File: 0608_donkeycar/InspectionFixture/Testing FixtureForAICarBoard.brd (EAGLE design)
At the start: 65 x 56.5 mm, 100 parts, among them CON1 RASPBERRYPI_SHEILD, CON2 5077CR-16-SMC2-BK-TR, U1 RP2350A, U2 W25Q32RVXHJQ, U3 TXB0104, U4 RT6150B-33GQW, U5 DMG1012T, U6 MCP3008

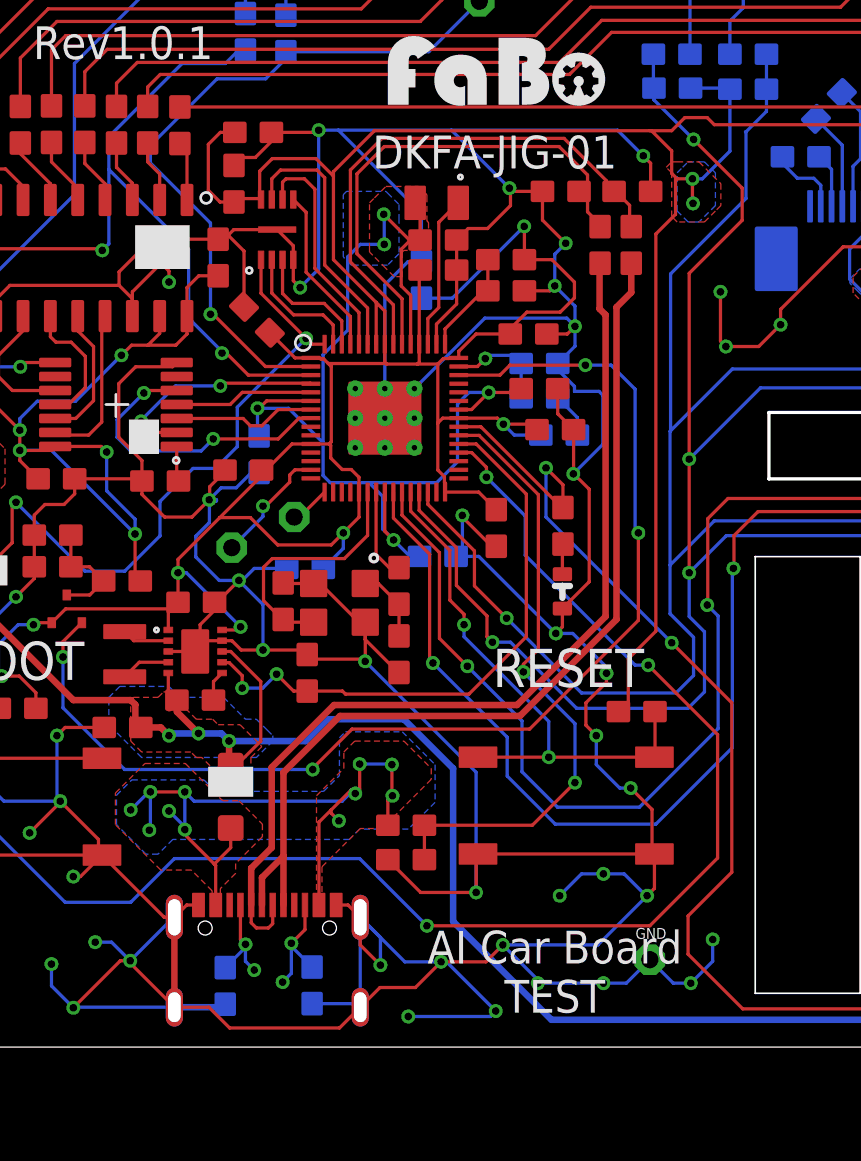
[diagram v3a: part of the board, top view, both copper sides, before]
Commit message: #608 AI Car Board Inspection Board Rev1.0.1 C34コンデンサ47uF追加、発振器マーキングポイント追加、アナログ系の電源の定数を変更、レベル変換A側電源断線修正
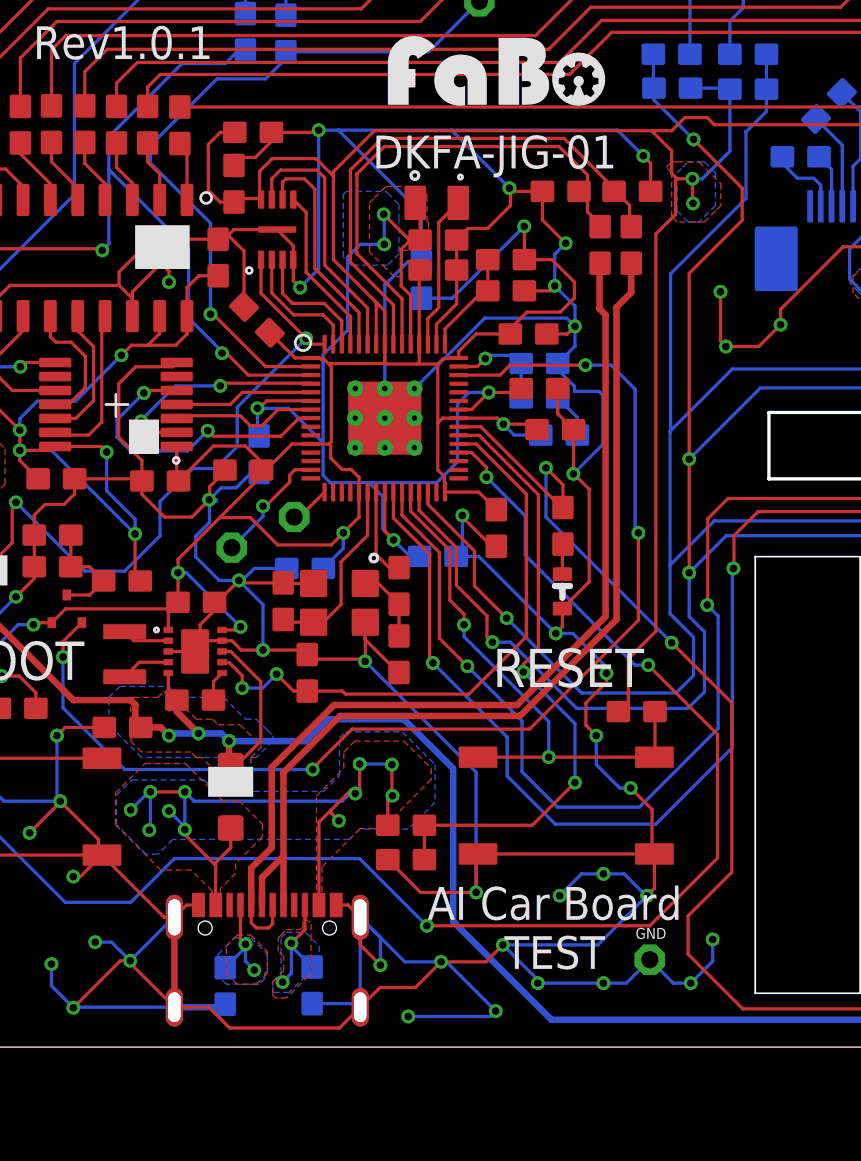
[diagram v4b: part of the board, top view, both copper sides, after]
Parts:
- R26: value 100K -> 200
- R27: value 100K -> 1
- R28: value 100K -> 33
- R29: value 10K -> 1K
- R30: value DNP -> 10K
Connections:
- removed net N$61: C13.2, U3.1
- net VSYS_3V3: now also C13.2, U3.1
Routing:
- net VSYS_3V3: track 246.9 -> 253.7 mm
- net OSC-IN: track 11.8 -> 8.86 mm
- net N$61: track 1.64 -> 0.00 mm
- added copper zone on layer 1, net N$1
- added copper zone on layer 16, net N$1
- added copper zone on layer 1, net N$2
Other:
- board text added: "Testing Jig For AI Car Board Rev1.0.1 2025/05/19 DKFA-JIG-01"
- board text removed: "Testing Jig For AI Car Board Rev1.0.1 2025/04/17 DKFA-JIG-01"

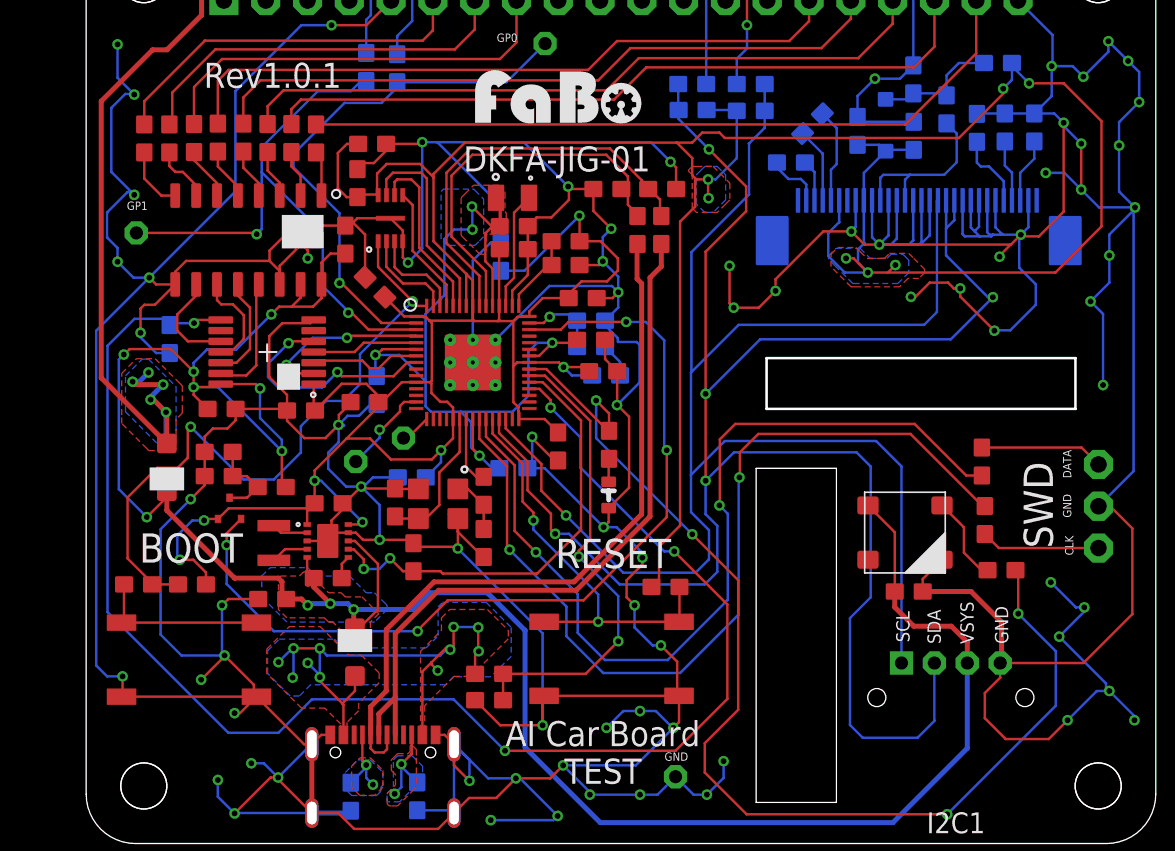
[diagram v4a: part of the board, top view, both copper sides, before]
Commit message: #608 AI Car Board検査治具アップデート　ダイオード追加
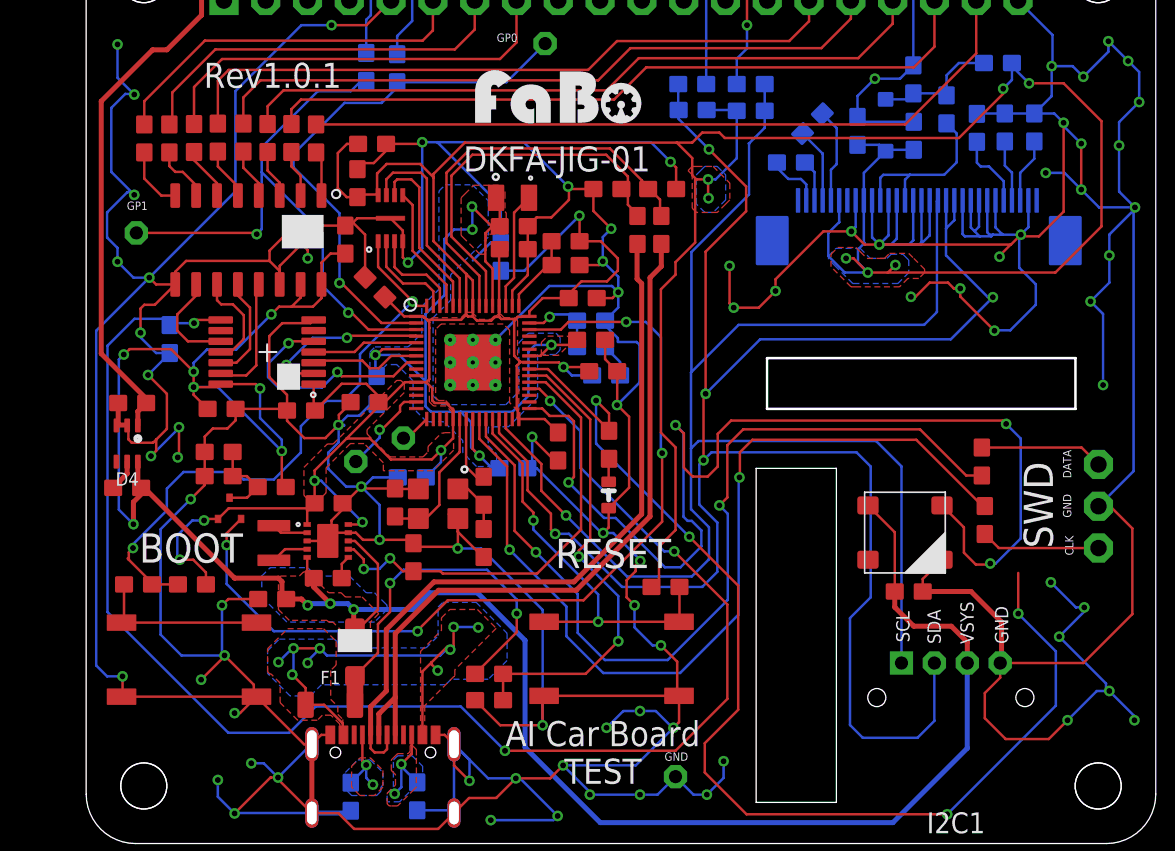
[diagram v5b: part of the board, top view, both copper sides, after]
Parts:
- removed D3: PMEG6010ELR-Q, FaBo-Diode:SOD123W
- removed R39: DNP, FaBo-Resistors:0603-BOTTOM
- added C35: 0.1uF, FaBo-Capacitor:0603-BOTTOM
- added D4: (no value), FaBo-Diode:SC-70
- added F1: (no value), FaBo-Supply:1206
- added LOGO2: (no value), component:LOGO_FABO_M
- added R40: 10K, FaBo-Resistors:0603
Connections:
- removed net 5V: CON1.2, D3.2
- removed net N$3: LED2.4-DIN, R39.1
- new net 5V2: C35.2, CON1.2, D4.1
- new net GPIO21: LED2.4-DIN, U1.31
- new net N$6: D4.5, R40.1
- new net VBUS-2: D2.2, F1.2, R5.2
- net GND: now also C35.1, D4.2, D4.3
- net GP25: no longer R39.2
- net VBUS: now also F1.1; no longer D2.2, R5.2
- net VSYS: now also D4.6, R40.2; no longer D3.1
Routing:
- net GPIO21: track 0.00 -> 66.2 mm, vias 0 -> 4
- net 5V: track 44.3 -> 0.00 mm, vias 5 -> 0
- net 5V2: track 0.00 -> 33.3 mm
- net VBUS-2: track 0.00 -> 22.6 mm, vias 0 -> 2
- net GND: track 749.7 -> 762.3 mm, vias 80 -> 84
- net VBUS: track 34.7 -> 29.4 mm, vias 11 -> 9
- net N$3: track 5.30 -> 0.00 mm
- net QSPI-SS: track 40.9 -> 36.6 mm
- net VSYS: track 149.3 -> 152.0 mm
- net N$6: track 0.00 -> 1.94 mm
- net VSYS_3V3: track 253.7 -> 254.9 mm
- net SWD: track 54.2 -> 53.5 mm
- removed copper zone on layer 1, net 5V
- removed copper zone on layer 16, net 5V
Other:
- board text added: "Not for sale"
- board text added: "S/N"
- board text added: "Testing Jig For AI Car Board Rev1.0.1 2025/06/05 DKFA-JIG-01"
- board text removed: "Testing Jig For AI Car Board Rev1.0.1 2025/05/19 DKFA-JIG-01"
